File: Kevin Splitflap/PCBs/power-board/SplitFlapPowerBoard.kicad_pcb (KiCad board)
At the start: 2 copper layers, 157 x 25.5 mm, 40 parts, among them J1 KPJX-4S-S, J10 ROCKER SWITCH, J2 ROW 1 (12V B A GND), J3 ROW 2 (12V B A GND), J4 ROW 3 (12V B A GND), J5 GATEWAY PWR (12V GND), J6 GATEWAY RS485 (A B), J7 GATEWAY IO, J8 LED START (12V DIN BIN GND), J9 LED END (12V GND), U1 74AHCT1G125, U2 78L05

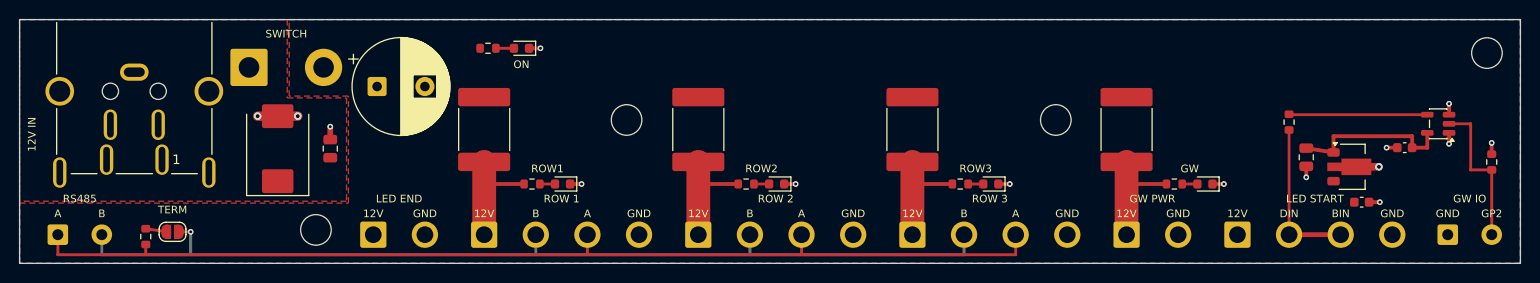
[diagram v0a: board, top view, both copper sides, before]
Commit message: Power board: jack/switch to the right end, fix DIN jack pinout and position, add rework links
- Mirror the layout left-right: KPJX-4S-S jack and rocker pads at the top-right
  (bottom-left when turned over), wire pads along the bottom edge.
- Jack pinout per Mean Well's R7B plug-face drawing: Kycon pins 2+4 = +12 V,
  1+3 = GND (same side, not diagonal; Mean Well numbers its plug differently).
- Move the jack 4 mm toward the edge so the body face sits on the board edge
  and the 4 mm barrel passes through the panel; fix the footprint outline.
- Jack pin pairs get their own copper, joined to +12V_IN / GND by cuttable
  net-tie links (NT1, NT2) between 16 AWG solder holes, so a reversed plug
  can be fixed with two cuts and two wires. Instructions on the back silk.
- ERC/DRC clean with schematic parity; JLC gerbers, BOM and CPL regenerated.
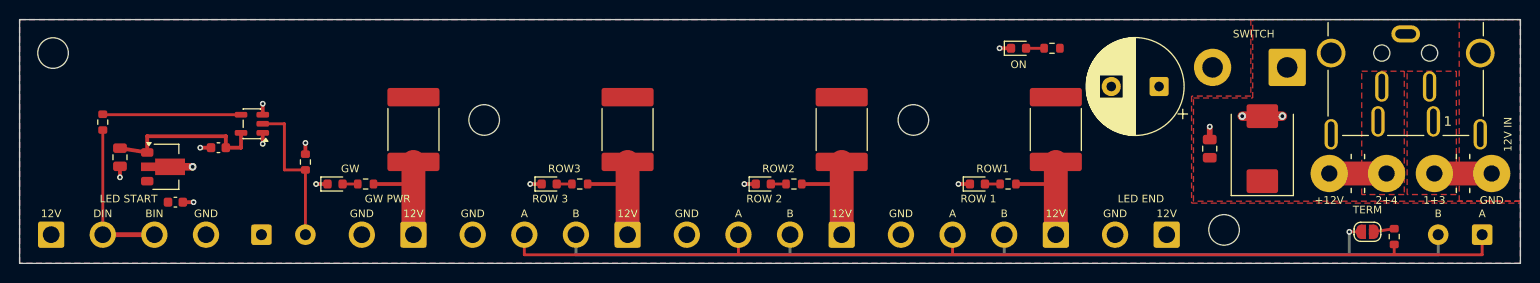
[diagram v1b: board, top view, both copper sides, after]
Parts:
- added NT1: CUT IF REVERSED, PowerBoard:CutLink_Holes_P6mm, F.Cu at (140.0, 16.1)
- added NT2: CUT IF REVERSED, PowerBoard:CutLink_Holes_P6mm, F.Cu at (151.0, 16.1)
- moved H4 150.0 mm to (3.50, 3.50)
- moved J6 149.0 mm to (153.0, 22.5), turned to 180 degrees
- moved J1 133.1 mm to (145.0, 3.50)
- moved R7 130.6 mm to (143.8, 22.7)
- moved JP1 125.0 mm to (141.0, 22.2), turned to 0 degrees
- moved C3 124.1 mm to (20.8, 13.4)
- moved C4 124.1 mm to (16.3, 19.1)
- moved J7 124.1 mm to (25.3, 22.5)
- moved J8 124.1 mm to (3.30, 22.5)
- moved R9 124.1 mm to (8.70, 10.7)
- moved U1 124.1 mm to (24.3, 10.9)
- moved U2 124.1 mm to (15.3, 15.4)
- moved C5 124.1 mm to (10.5, 14.4)
- moved R8 124.1 mm to (29.9, 14.9)
- moved J10 108.6 mm to (132.6, 5.00), turned to 180 degrees
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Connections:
- J1 pad 1: /+12V_IN -> /JACK_13
- J1 pad 2: /GND -> /JACK_24
- J1 pad 3: /GND -> /JACK_13
- J1 pad 4: /+12V_IN -> /JACK_24
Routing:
- added copper zone on F.Cu, net /GND
- added copper zone on F.Cu, net /JACK_13
- added copper zone on F.Cu, net /JACK_24
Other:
- board text added: "+12V"
- board text added: "1+3"
- board text added: "2+4"
- board text added: "JACK PLUG REVERSED? CUT BOTH LINKS ON THE FRONT,"
- board text added: "THEN WIRE PIN 1+3 -> +12V AND PIN 2+4 -> GND (16 AWG)"
- board text removed: "GP2"
- board text removed: "GW IO"
- board text removed: "RS485"
